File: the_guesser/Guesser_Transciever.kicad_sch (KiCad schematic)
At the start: 51 parts, among them J2 Conn_Coaxial, J3 RFShield_TwoPieces, U5 CC1101RGPR, U6 CC1190RGVR, U7 B39921B3728U410, X1 STDCRG2-27M

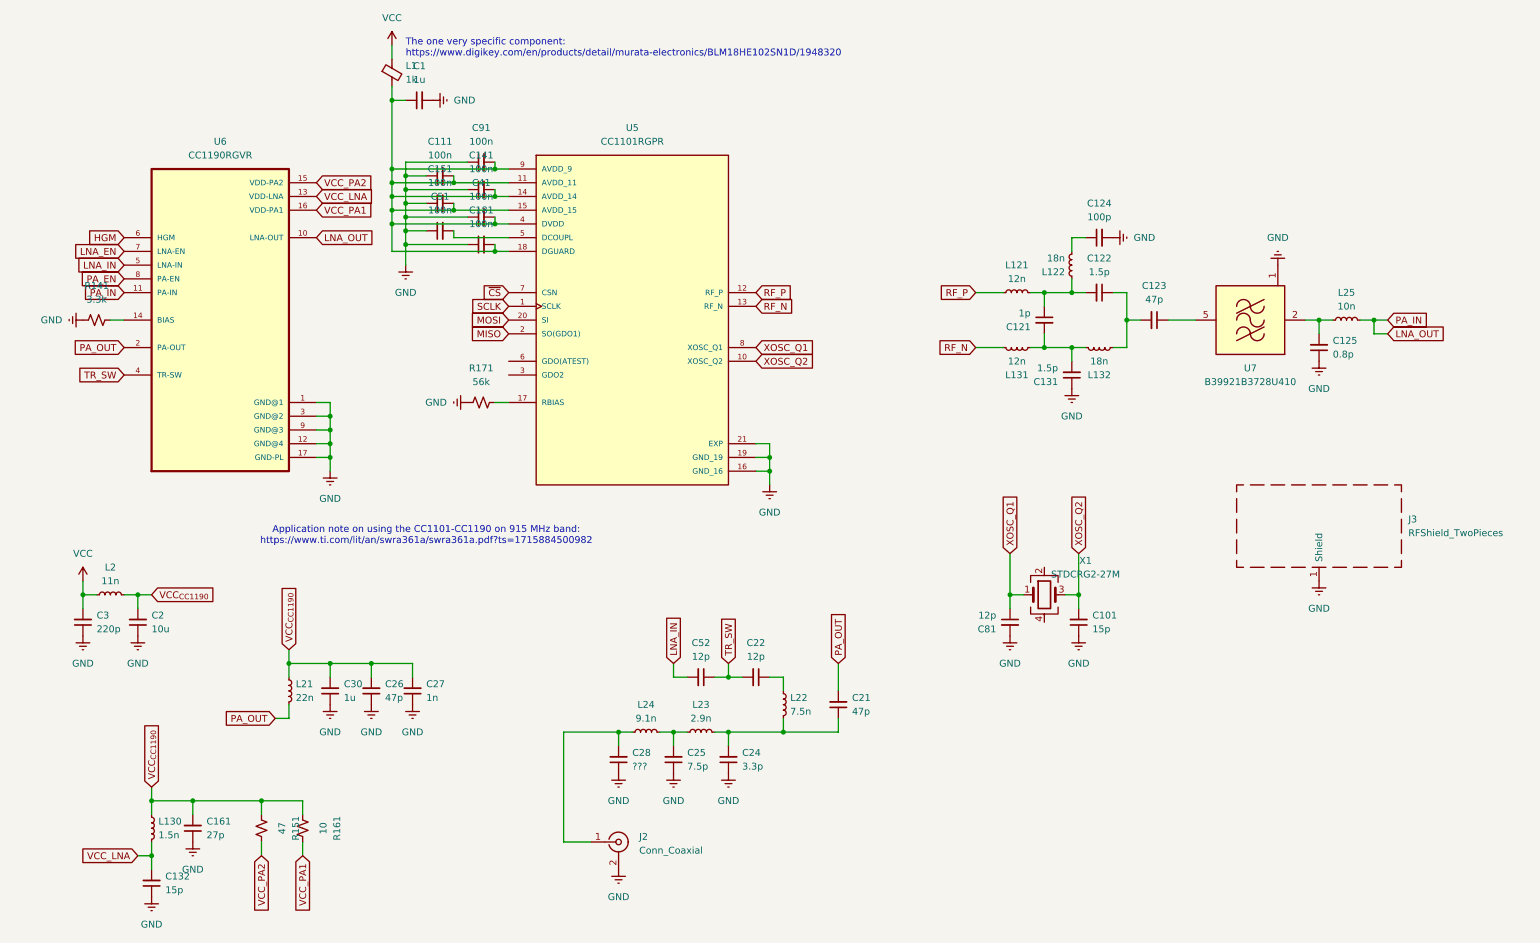
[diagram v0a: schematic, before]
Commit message: Routed Guesser RF components
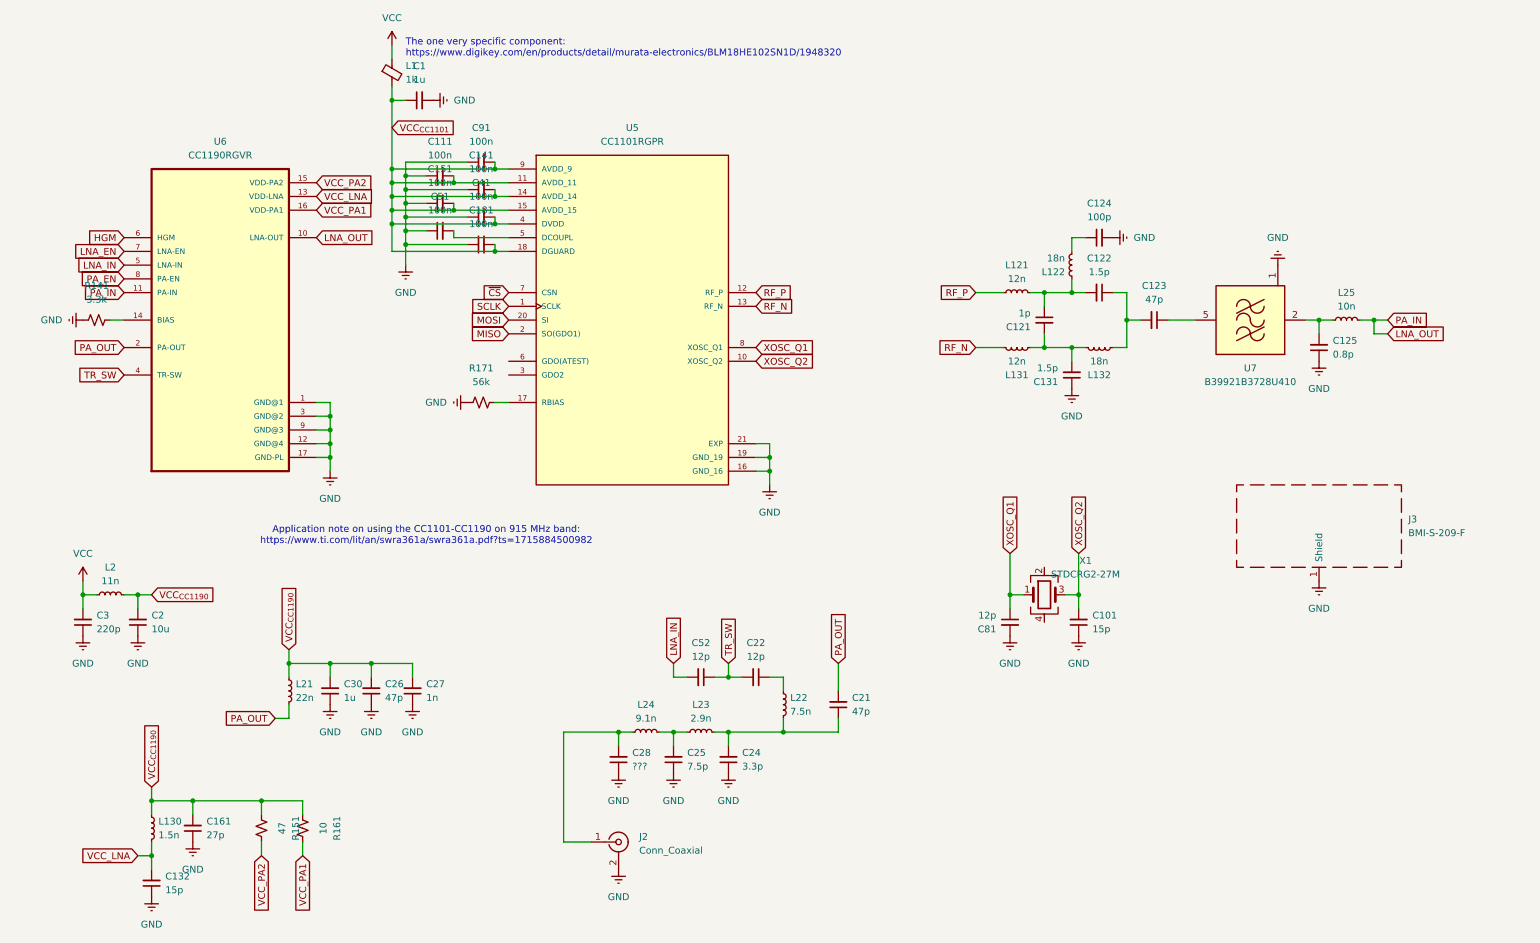
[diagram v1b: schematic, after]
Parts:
- J3: value RFShield_TwoPieces -> BMI-S-209-F; DKPN (none) -> 903-1212-1-ND
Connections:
- net VCC_{CC1101}: now reaches C1.1, C111.2, C141.2, C151.2, C181.2, C41.2, C91.2, L1.2, U5.11 (AVDD_11), U5.14 (AVDD_14), U5.15 (AVDD_15), U5.18 (DGUARD), U5.4 (DVDD), U5.9 (AVDD_9)
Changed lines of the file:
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@@
 		)
 	)
+	(global_label "VCC_{CC1101}"
+		(shape input)
+		(at 82.55 40.64 0)
+		(fields_autoplaced yes)
+		(effects
+			(font
+				(size 1.27 1.27)
+			)
+			(justify left)
+		)
+		(property "Intersheetrefs" "${INTERSHEET_REFS}"
+			(at 95.117 40.64 0)
+			(effects
+				(font
+					(size 1.27 1.27)
+				)
+				(justify left)
+				(hide yes)
+			)
+		)
+	)
 	(global_label "HGM"
 		(shape input)
@@
 			)
 		)
-		(property "Value" "RFShield_TwoPieces"
+		(property "Value" "BMI-S-209-F"
 			(at 270.51 115.5699 0)
 			(effects
@@
 			)
 		)
+		(property "DKPN" "903-1212-1-ND"
+			(at 254 114.3 0)
+			(effects
+				(font
+					(size 1.27 1.27)
+				)
+				(hide yes)
+			)
+		)
 		(pin "1"
 		)
@@
 		(exclude_from_sim no)
 		(in_bom yes)
-		(on_board yes)
+		(on_board no)
 		(dnp no)
 		(fields_autoplaced yes)

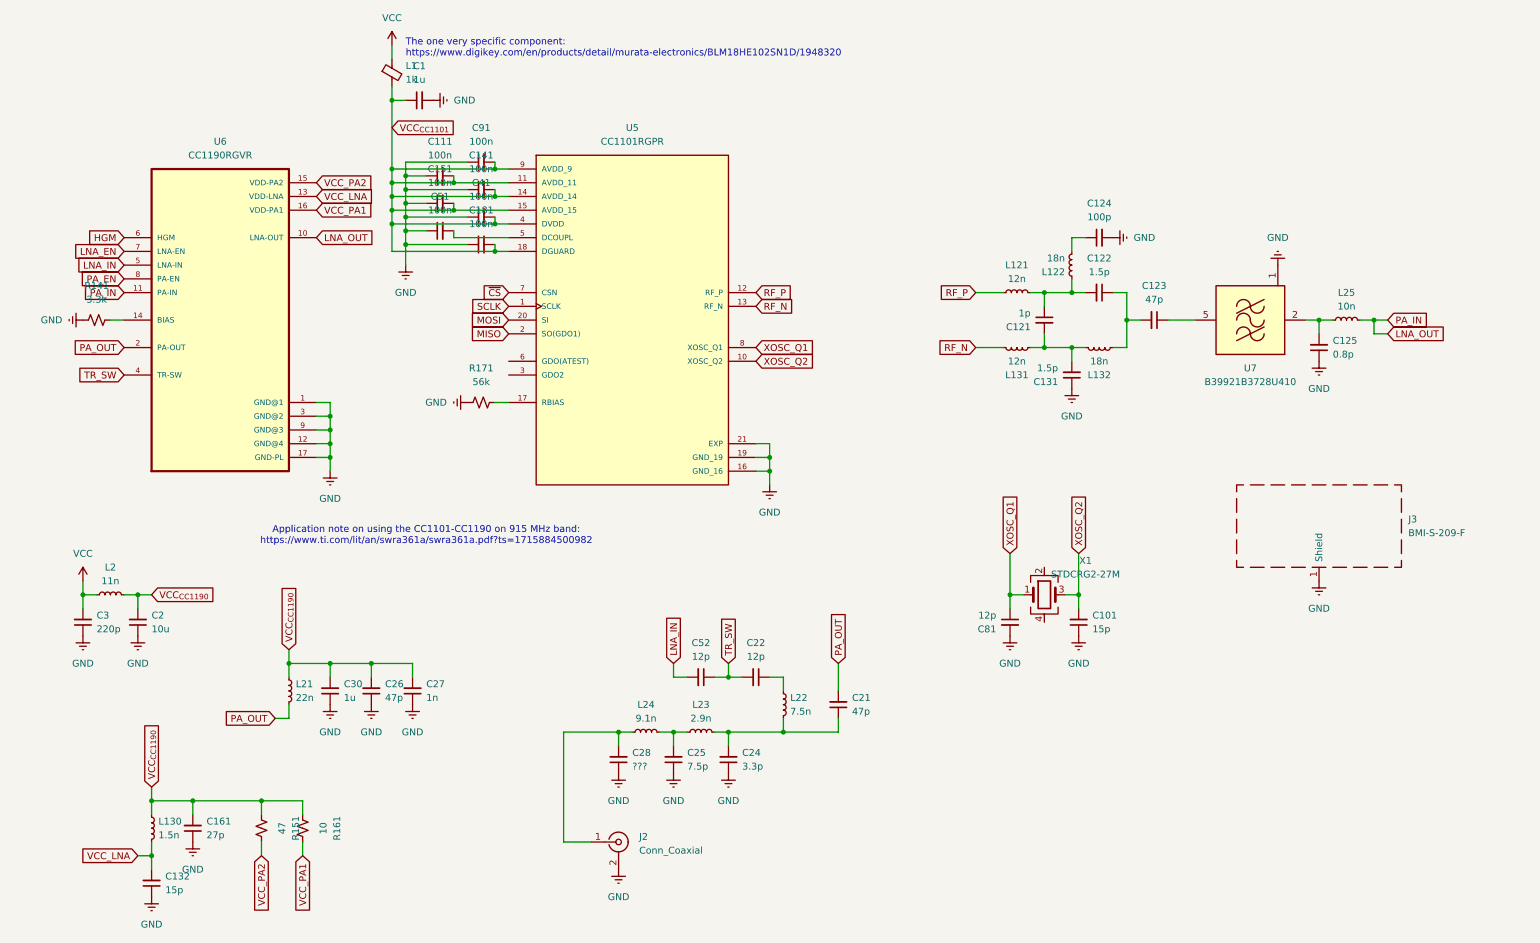
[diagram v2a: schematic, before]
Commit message: Started Guesser I/O and continued sensor selection
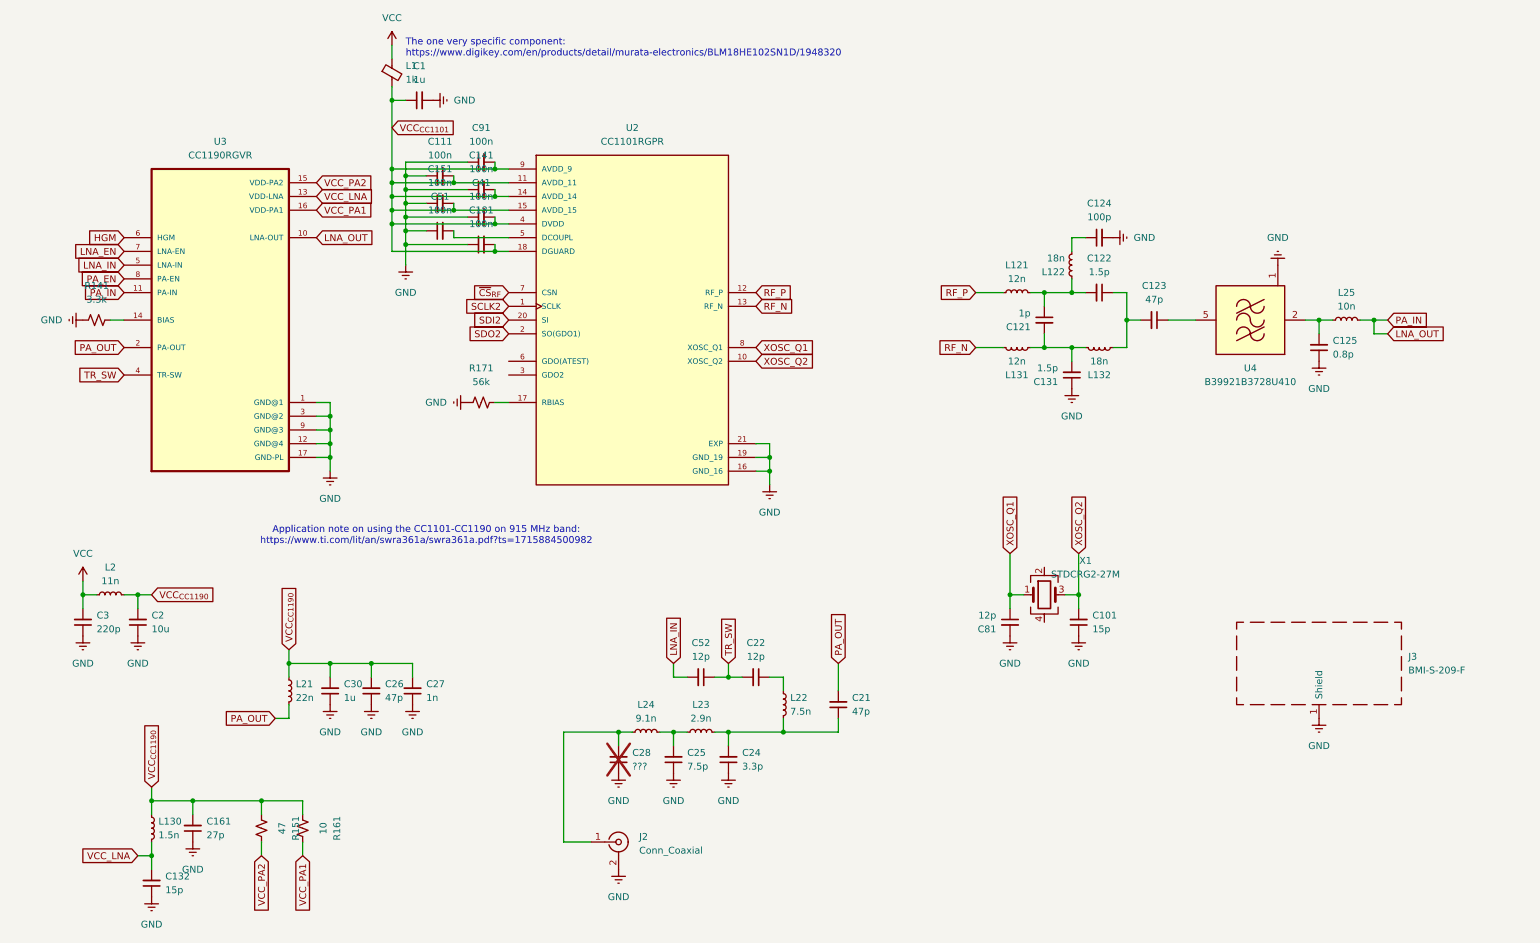
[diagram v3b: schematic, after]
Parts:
- C28: now not fitted
- renumbered U5 to U2, U6 to U3, U7 to U4
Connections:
- net MISO renamed SDO2
- net MOSI renamed SDI2
- net SCLK renamed SCLK2
- net ~{CS} renamed ~{CS}_{RF}
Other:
- moved on the sheet: J3
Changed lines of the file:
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@@
 		)
 	)
-	(global_label "MISO"
+	(global_label "SDO2"
 		(shape input)
 		(at 104.14 78.74 180)
@@
 		)
 	)
-	(global_label "SCLK"
+	(global_label "SCLK2"
 		(shape input)
 		(at 104.14 73.66 180)
@@
 		)
 	)
-	(global_label "~{CS}"
+	(global_label "~{CS}_{RF}"
 		(shape input)
 		(at 104.14 71.12 180)
@@
 		)
 		(property "Intersheetrefs" "${INTERSHEET_REFS}"
-			(at 98.6753 71.12 0)
+			(at 96.7376 71.12 0)
 			(effects
 				(font
@@
 		)
 	)
-	(global_label "MOSI"
+	(global_label "SDI2"
 		(shape input)
 		(at 104.14 76.2 180)
@@
 	(symbol
 		(lib_id "power:Earth")
-		(at 254 124.46 0)
+		(at 254 149.86 0)
 		(unit 1)
 		(exclude_from_sim no)
@@
 		(fields_autoplaced yes)
 		(property "Reference" "#PWR044"
-			(at 254 130.81 0)
+			(at 254 156.21 0)
 			(effects
 				(font
@@
 		)
 		(property "Value" "GND"
-			(at 254 129.54 0)
+			(at 254 154.94 0)
 			(effects
 				(font
@@
 		)
 		(property "Footprint" ""
-			(at 254 124.46 0)
+			(at 254 149.86 0)
 			(effects
 				(font
@@
 		)
 		(property "Datasheet" "~"
-			(at 254 124.46 0)
+			(at 254 149.86 0)
 			(effects
 				(font
@@
 		)
 		(property "Description" "Power symbol creates a global label with name \"Earth\""
-			(at 254 124.46 0)
+			(at 254 149.86 0)
 			(effects
 				(font
@@
 		(dnp no)
 		(fields_autoplaced yes)
-		(property "Reference" "U6"
+		(property "Reference" "U3"
 			(at 50.8 43.18 0)
 			(effects
@@
 			(project "the_guesser"
 				(path "/473e3a2e-6c5e-4995-af4a-e4bf1449cab0/144203ce-f59d-4228-a9f3-243b499459b2"
-					(reference "U6")
+					(reference "U3")
 					(unit 1)
 				)
@@
 		(dnp no)
 		(fields_autoplaced yes)
-		(property "Reference" "U5"
+		(property "Reference" "U2"
 			(at 127 40.64 0)
 			(effects
@@
 			(project "the_guesser"
 				(path "/473e3a2e-6c5e-4995-af4a-e4bf1449cab0/144203ce-f59d-4228-a9f3-243b499459b2"
-					(reference "U5")
+					(reference "U2")
 					(unit 1)
 				)
@@
 		(dnp no)
 		(fields_autoplaced yes)
-		(property "Reference" "U7"
+		(property "Reference" "U4"
 			(at 241.3 85.09 0)
 			(effects
@@
 			(project "the_guesser"
 				(path "/473e3a2e-6c5e-4995-af4a-e4bf1449cab0/144203ce-f59d-4228-a9f3-243b499459b2"
-					(reference "U7")
+					(reference "U4")
 					(unit 1)
 				)
@@
 	(symbol
 		(lib_id "Device:RFShield_OnePiece")
-		(at 254 114.3 0)
+		(at 254 139.7 0)
 		(unit 1)
 		(exclude_from_sim no)
@@
 		(fields_autoplaced yes)
 		(property "Reference" "J3"
-			(at 270.51 113.0299 0)
+			(at 270.51 138.4299 0)
 			(effects
 				(font
@@
 		)
 		(property "Value" "BMI-S-209-F"
-			(at 270.51 115.5699 0)
+			(at 270.51 140.9699 0)
 			(effects
 				(font
@@
 		)
 		(property "Footprint" "RF_Shielding:Laird_Technologies_BMI-S-209-F_29.36x18.50mm"
-			(at 254 116.84 0)
+			(at 254 142.24 0)
 			(effects
 				(font
@@
 		)
 		(property "Datasheet" "~"
-			(at 254 116.84 0)
+			(at 254 142.24 0)
 			(effects
 				(font
@@
 		)
 		(property "Description" "One-piece EMI RF shielding cabinet"
-			(at 254 114.3 0)
+			(at 254 139.7 0)
 			(effects
 				(font
@@
 		)
 		(property "DKPN" "903-1212-1-ND"
-			(at 254 114.3 0)
+			(at 254 139.7 0)
 			(effects
 				(font
@@
 		(in_bom yes)
 		(on_board yes)
-		(dnp no)
+		(dnp yes)
 		(fields_autoplaced yes)
 		(property "Reference" "C28"
